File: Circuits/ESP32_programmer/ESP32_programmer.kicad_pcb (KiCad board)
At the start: 4 copper layers, 23.4 x 25.8 mm, 16 parts, among them J1 Conn_01x06_Pin, J2 USB_C_Receptacle_USB2.0_14P, Q2 MMDT3904, U1 TPD4S014, U7 CP2102N-Axx-xQFN24

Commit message: Full redesign of connector board, including removal of USB flashing. This is now done by the flasher board.
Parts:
- removed R16, R17: 10k, Resistor_SMD:R_0603_1608Metric_Pad0.98x0.95mm_HandSolder
- R3, R4: value 1k -> 10k
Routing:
- net GND: track 27.5 -> 23.7 mm, vias 4 -> 3
- net /ESP_EN: track 13.8 -> 10.8 mm
- net /ESP_IO0: track 17.2 -> 14.1 mm

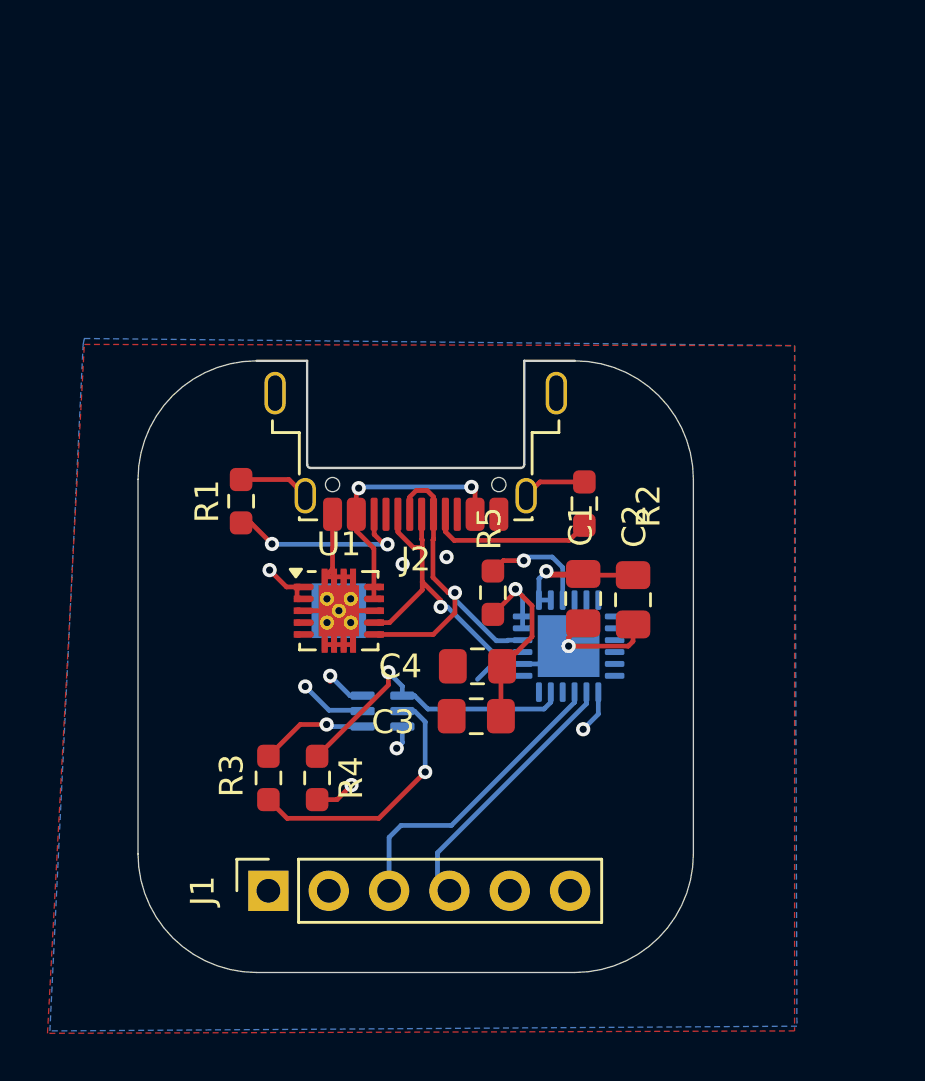
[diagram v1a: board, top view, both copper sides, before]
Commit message: Added LEDs to the programmer
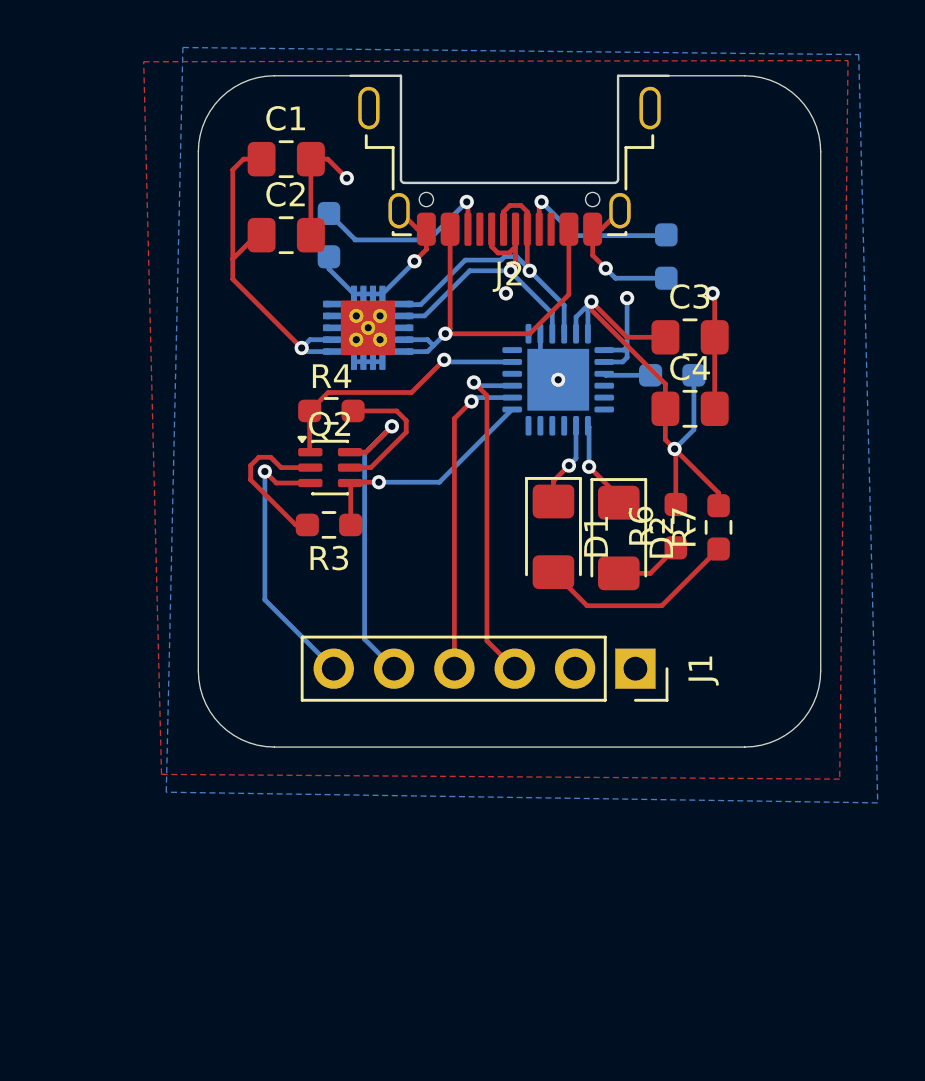
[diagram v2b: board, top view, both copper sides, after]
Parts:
- added D1: LED, LED_SMD:LED_1206_3216Metric_Pad1.42x1.75mm_HandSolder, F.Cu at (58.6, 51.2)
- added D2: LED, LED_SMD:LED_1206_3216Metric_Pad1.42x1.75mm_HandSolder, F.Cu at (61.4, 51.3)
- added R6: 500, Resistor_SMD:R_0603_1608Metric_Pad0.98x0.95mm_HandSolder, F.Cu at (63.8, 50.8)
- added R7: 500, Resistor_SMD:R_0603_1608Metric_Pad0.98x0.95mm_HandSolder, F.Cu at (65.5, 50.9)
- Q2: moved to F.Cu
- R1, R2, R5, U1: moved to B.Cu
- moved C1 22.3 mm to (47.4, 35.4), turned to 0 degrees
- moved C2 21.2 mm to (47.4, 38.5), turned to 0 degrees
- moved C3 18.3 mm to (64.3, 42.9), turned to 0 degrees
- moved J1 18.1 mm to (62.0, 56.8), turned to -90 degrees
- moved R4 15.5 mm to (49.2, 46.0), turned to 0 degrees
- moved C4 14.1 mm to (64.3, 45.9), turned to 0 degrees
- moved J2 12.6 mm to (56.8, 33.2)
- moved U1 12.0 mm to (50.8, 42.5)
- moved R5 11.9 mm to (63.6, 44.5), turned to 0 degrees
- moved R1 11.8 mm to (49.1, 38.5), turned to -90 degrees
- moved U7 11.2 mm to (58.8, 44.6), turned to -90 degrees
- moved R2 11.0 mm to (63.4, 39.5), turned to -90 degrees
- moved R3 11.0 mm to (49.1, 50.8), turned to 180 degrees
- moved Q2 10.5 mm to (49.2, 48.3), turned to 0 degrees
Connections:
- net Net-(U7-VDD) renamed /3v3
- U7 pad 13: unconnected-(U7-~{RXT}/GPIO.1-Pad13) -> Net-(D2-K)
- U7 pad 14: unconnected-(U7-~{TXT}/GPIO.0-Pad14) -> Net-(D1-K)
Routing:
- net /3v3: track 9.42 -> 23.4 mm, vias 1 -> 2
- net /VCC: track 9.39 -> 18.9 mm
- net Net-(D1-A): track 0.00 -> 8.52 mm
- net /RTS: track 17.3 -> 9.88 mm, vias 2 -> 1
- net GND: track 23.7 -> 30.6 mm, vias 3 -> 6
- net /USB_VBUS: track 11.7 -> 16.3 mm, vias 2 -> 1
- net Net-(Q2A-B1): track 11.0 -> 6.61 mm, vias 1 -> 0
- net Net-(D2-K): track 0.00 -> 3.78 mm, vias 0 -> 1
- net Net-(Q2B-B2): track 9.50 -> 5.88 mm, vias 2 -> 0
- net Net-(D1-K): track 0.00 -> 3.58 mm, vias 0 -> 1
- net Net-(D2-A): track 0.00 -> 2.85 mm
- net Net-(U7-~{RST}): track 4.74 -> 1.98 mm, vias 1 -> 0
- net /RX: track 11.2 -> 13.3 mm, vias 0 -> 1
- net /DTR: track 13.0 -> 11.2 mm
- net /TX: track 12.8 -> 14.4 mm, vias 0 -> 1
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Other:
- board size 23.4 x 25.8 mm -> 26.2 x 28.3 mm

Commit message: Update gitignore and I think I did some silkscreening
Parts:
- D1: value LED -> TX
- D2: value LED -> RX
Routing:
- net GND: track 30.6 -> 34.4 mm
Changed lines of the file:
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@@
 		)
 		(property "Value" "Conn_01x06_Pin"
-			(at 0 15.47 90)
+			(at -2.35 5.85 180)
 			(layer "F.Fab")
 			(effects
@@
 			(at 0 1.43 90)
 			(layer "F.Fab")
+			(hide yes)
 			(effects
 				(font
@@
 		(property "Value" "4.7uF"
 			(at 0 1.68 0)
-			(layer "F.Fab")
+			(layer "F.SilkS")
 			(effects
 				(font
@@
 			)
 		)
-		(property "Value" "LED"
-			(at 0 1.83 90)
-			(layer "F.Fab")
+		(property "Value" "TX"
+			(at -3.125601 0.44965 180)
+			(layer "F.SilkS")
 			(effects
 				(font
@@
 			)
 		)
-		(property "Value" "LED"
-			(at 0 1.83 90)
-			(layer "F.Fab")
+		(property "Value" "RX"
+			(at -3.243232 0.014236 180)
+			(layer "F.SilkS")
 			(effects
 				(font
@@
 		(tags "capacitor handsolder")
 		(property "Reference" "C2"
-			(at 0 -1.68 0)
+			(at -0.15 1.85 0)
 			(layer "F.SilkS")
 			(effects
@@
 		)
 		(property "Value" "0.1uF"
-			(at 0 1.68 0)
-			(layer "F.Fab")
+			(at -0.163569 3.14284 0)
+			(layer "F.SilkS")
 			(effects
 				(font
@@
 		)
 		(property "Value" "10k"
-			(at 0 1.43 0)
-			(layer "F.Fab")
+			(at -3.1 -0.1 0)
+			(layer "F.SilkS")
 			(effects
 				(font
@@
 		)
 		(property "Value" "500"
-			(at 0 1.43 90)
-			(layer "F.Fab")
+			(at -2.49012 -0.901948 180)
+			(layer "F.SilkS")
 			(effects
 				(font
@@
 		(property "Value" "4.7uF"
 			(at 0 1.68 0)
-			(layer "F.Fab")
+			(layer "F.SilkS")
 			(effects
 				(font
@@
 		)
 		(property "Value" "0.1uF"
-			(at 0 1.68 0)
-			(layer "F.Fab")
+			(at -3.997724 0.069855 0)
+			(layer "F.SilkS")
 			(effects
 				(font
@@
 		)
 		(property "Value" "10k"
-			(at 0 1.43 0)
-			(layer "F.Fab")
+			(at -2.85 0 0)
+			(layer "F.SilkS")
 			(effects
 				(font
@@
 		)
 		(property "Value" "MMDT3904"
-			(at 0 1.8 0)
+			(at 4.5 0.065 0)
 			(layer "F.Fab")
 			(effects
@@
 		(property "Value" "5.1k"
 			(at 0 -1.43 90)
-			(layer "B.Fab")
+			(layer "B.SilkS")
 			(effects
 				(font
@@
 		(property "Value" "1k"
 			(at 0 -1.43 0)
-			(layer "B.Fab")
+			(layer "B.SilkS")
 			(effects
 				(font
@@
 		(property "Value" "5.1k"
 			(at 0 -1.43 90)
-			(layer "B.Fab")
+			(layer "B.SilkS")
 			(effects
 				(font
@@
 	)
 	(segment
+		(start 51.3 42.95)
+		(end 50.3 41.95)
+		(width 0.2)
+		(layer "F.Cu")
+		(net "GND")
+	)
+	(segment
 		(start 65.3875 42.85)
 		(end 65.3875 41.0875)
@@
 	)
 	(segment
+		(start 51.3 41.95)
+		(end 51.3 42.95)
+		(width 0.2)
+		(layer "F.Cu")
+		(net "GND")
+	)
+	(segment
 		(start 65.3875 45.86)
 		(end 65.3875 42.85)
@@
 		(width 0.2)
 		(layer "F.Cu")
+		(net "GND")
+	)
+	(segment
+		(start 50.3 42.95)
+		(end 51.3 41.95)
+		(width 0.2)
+		(layer "F.Cu")
